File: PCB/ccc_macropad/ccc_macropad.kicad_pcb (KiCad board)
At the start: 2 copper layers, 101.5 x 44 mm, 17 parts, among them SW1 SW_Push, SW2 SW_Push, SW4 SW_Push, SW5 SW_Push, U1 RP2040-Zero

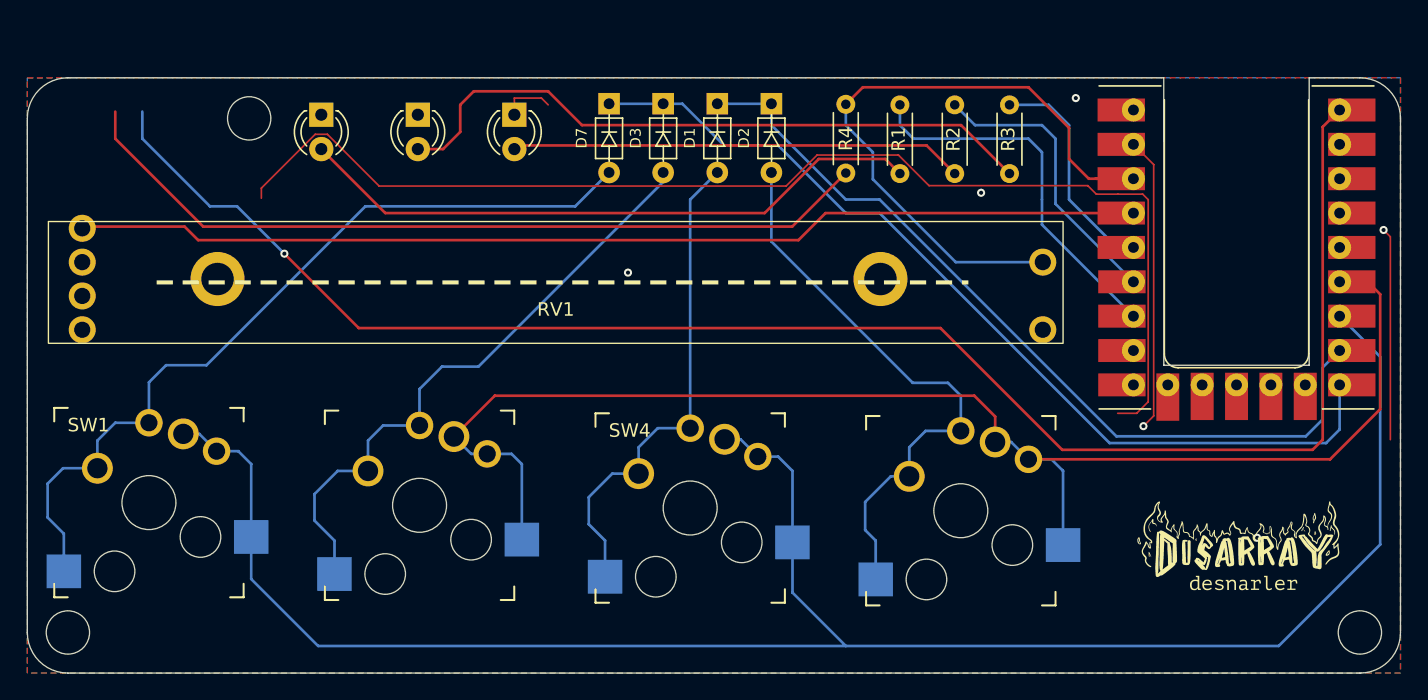
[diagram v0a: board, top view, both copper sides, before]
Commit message: fix: bigger traces/ more clearance
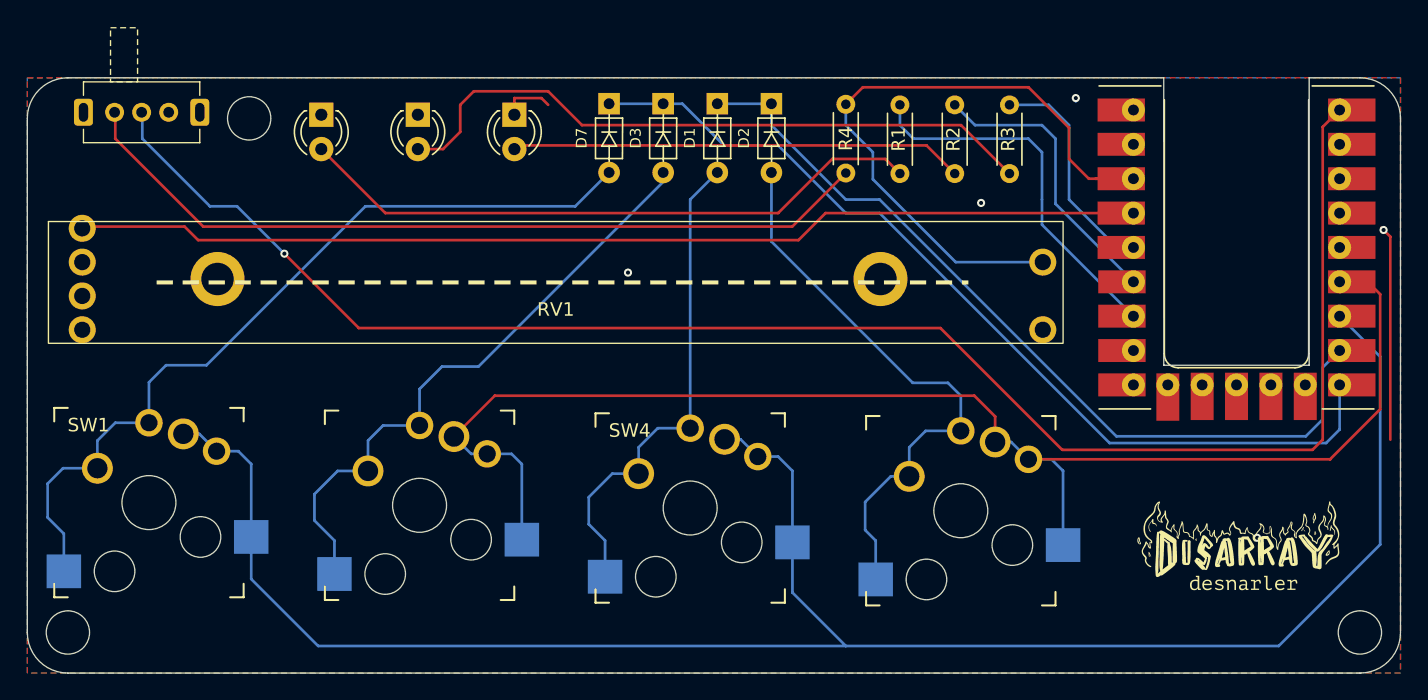
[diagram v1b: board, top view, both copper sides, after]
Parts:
- added SW3: OS/Left_Right-hand_Switch, CustomFootprints:SPDT_3pin_2_pos_1P2T_tht_2.54mm_switch_sk12d07, F.Cu at (114.7, 38.3)
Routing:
- net (no net): track 89.4 -> 0.00 mm
- net GND: track 42.4 -> 20.4 mm, vias 6 -> 5
